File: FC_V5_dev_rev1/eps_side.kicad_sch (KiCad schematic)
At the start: 81 parts, among them IC6 LT3652IMSE#PBF, J10 INHIBIT_P2, J13 Bypass, J14 Battery Input, J15 Heater, J19 ISS_INHIBIT, J20 ISS_INHIBIT, J24 Face0, J25 Face1, J26 Face2, J27 Face4, J28 Face4, J29 INHIBIT_S2, J7 INHIBIT_P1, J8 INHIBIT_S1, Q4 FDMQ86530L, Q7 DMP2240UDM-7, Q8 DMP2240UDM-7, U10 TPS54226PWPRPWP14_2P31X2P46-L, U13 TPS7A4501DCQT, U14 INA219AxD, U15 INA219AxD, U17 LMC555CMX/NOPB, U18 SN74HC595DR, U20 74LVC1G04

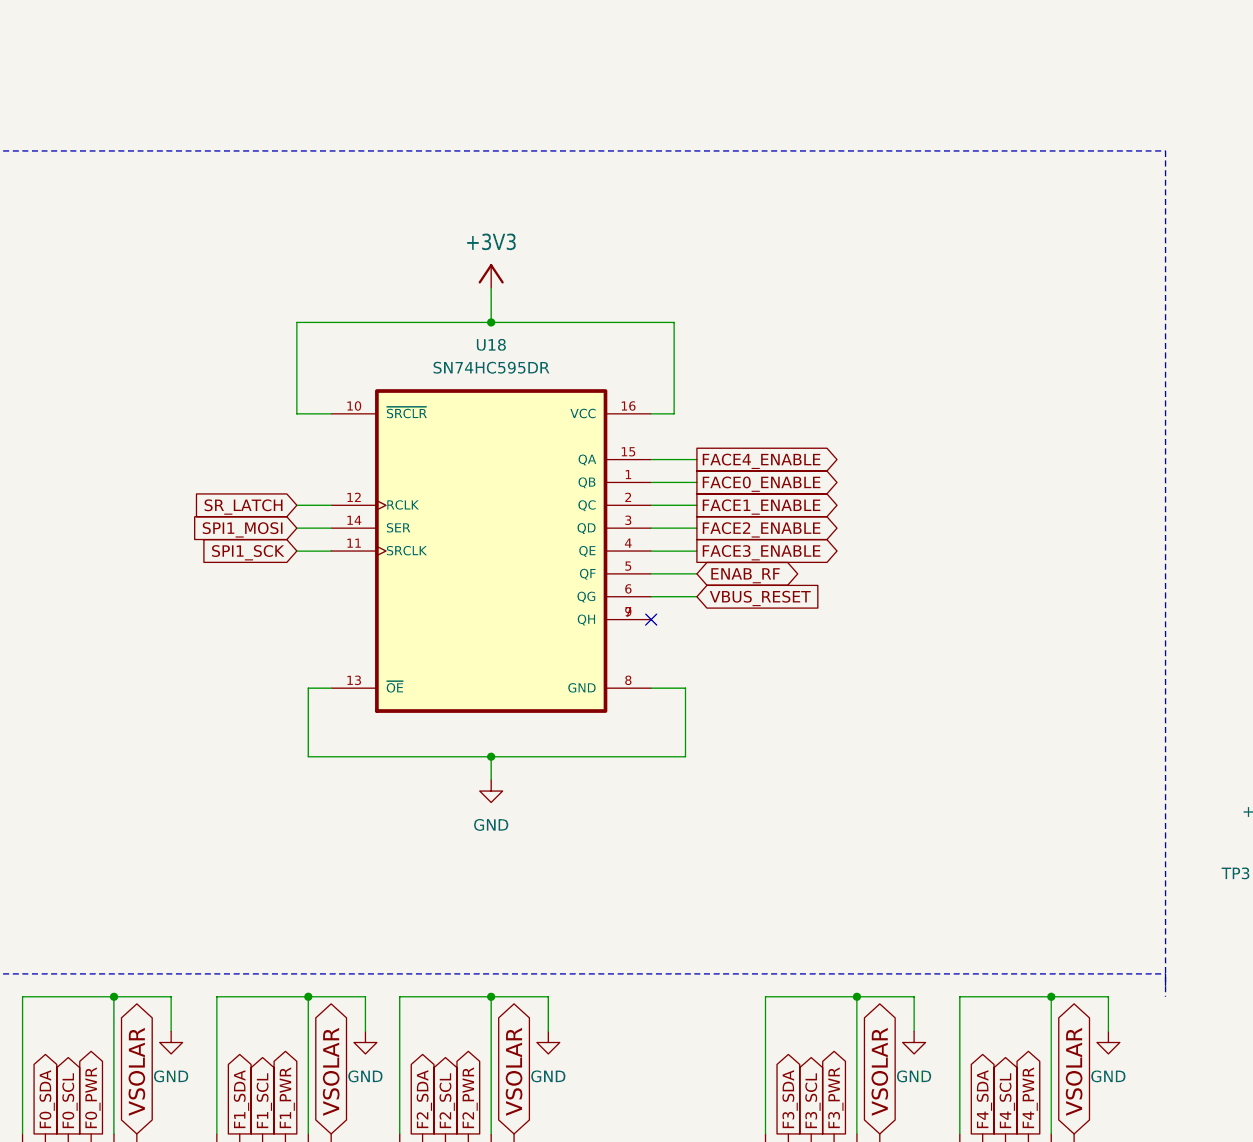
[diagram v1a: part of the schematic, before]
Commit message: Reorganized Schematic
Now with more sheets than ever!
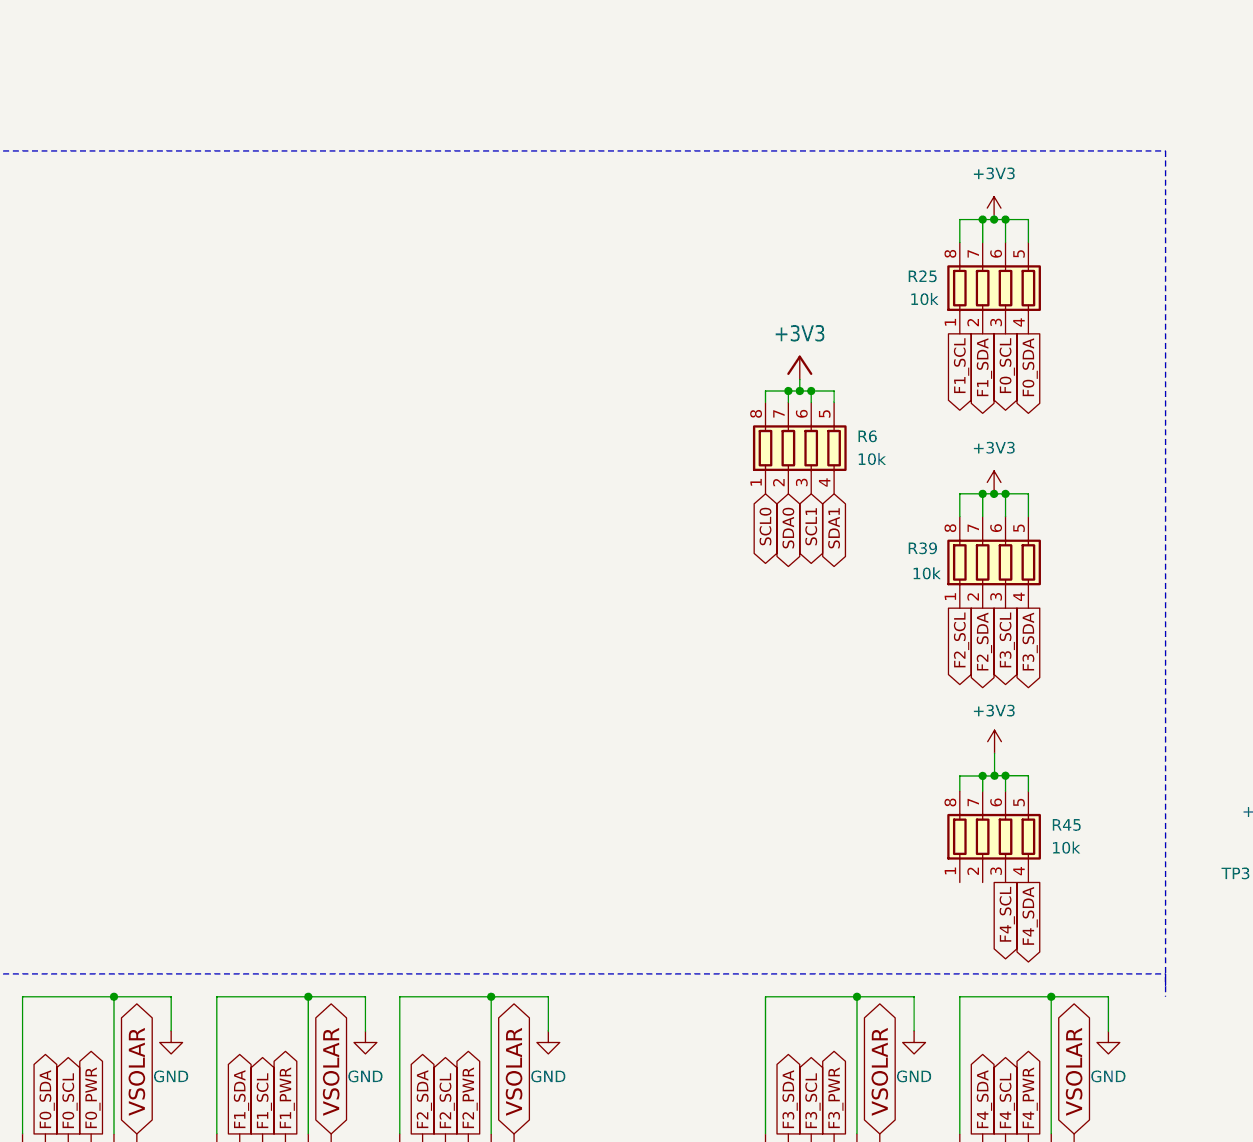
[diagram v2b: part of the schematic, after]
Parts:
- removed U18: SN74HC595DR, SN74HC595DR:SOIC127P600X175-16N, symbol SN74HC595:SN74HC595DR
- added R25, R39, R45, R6: 10k, Resistor_SMD:R_Array_Convex_4x0603, symbol Device:R_Pack04
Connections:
- net +3V3: now also R25.5 (R4.2), R25.6 (R3.2), R25.7 (R2.2), R25.8 (R1.2), R39.5 (R4.2), R39.6 (R3.2), R39.7 (R2.2), R39.8 (R1.2), R45.5 (R4.2), R45.6 (R3.2), R45.7 (R2.2), R45.8 (R1.2), R6.5 (R4.2), R6.6 (R3.2), R6.7 (R2.2), R6.8 (R1.2)
- net F0_SCL: now also R25.3 (R3.1)
- net F0_SDA: now also R25.4 (R4.1)
- net F1_SCL: now also R25.1 (R1.1)
- net F1_SDA: now also R25.2 (R2.1)
- net F2_SCL: now also R39.1 (R1.1)
- net F2_SDA: now also R39.2 (R2.1)
- net F3_SCL: now also R39.3 (R3.1)
- net F3_SDA: now also R39.4 (R4.1)
- net F4_SCL: now also R45.3 (R3.1)
- net F4_SDA: now also R45.4 (R4.1)
- net SCL1: now also R6.3 (R3.1)
- net SDA1: now also R6.4 (R4.1)
- new net SCL0: R6.1 (R1.1)
- new net SDA0: R6.2 (R2.1)
- no-connect marks 7 -> 6

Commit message: Return of the Shift Register
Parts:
- removed J24: Face0, Molex 6 pos:MOLEX_5040500691, symbol Connector_Generic:Conn_01x06
- removed J25: Face1, Molex 6 pos:MOLEX_5040500691, symbol Connector_Generic:Conn_01x06
- removed J26: Face2, Molex 6 pos:MOLEX_5040500691, symbol Connector_Generic:Conn_01x06
- removed J27, J28: Face4, Molex 6 pos:MOLEX_5040500691, symbol Connector_Generic:Conn_01x06
